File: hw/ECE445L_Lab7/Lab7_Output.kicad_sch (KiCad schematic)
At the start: 4 parts, among them Q1 IRLD024PBF, U2 Adafruit ST7735R

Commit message: finished preliminary pin assignment
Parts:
- removed Q1: IRLD024PBF, ECE445L:DIP920W60P254L490H457Q4N, symbol ECE445L:IRLD024PBF
- added M1, M2, M3, M4: Motor_DC, symbol Motor:Motor_DC
- added Q1, Q2, Q3, Q4: NTR4501NT1G, ECE445L:SOT96P237X111-3N, symbol ECE445L:NTR4501NT1G
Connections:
- new net: M3.2 (-), Q3.3 (D)
- new net: M4.2 (-), Q4.3 (D)
- new net: M2.2 (-), Q2.3 (D)
- new net: M1.2 (-), Q1.3 (D)
- new net GNDPWR: Q1.2 (S), Q2.2 (S), Q3.2 (S), Q4.2 (S)
- new net V_{g}: M1.1 (+), M2.1 (+), M3.1 (+), M4.1 (+)

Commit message: work on schem
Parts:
- added M5, M6: Motor_DC, symbol Motor:Motor_DC
- added M7: Solenoid_DC, symbol Motor:Motor_DC
- added Q5: NTR4501NT1G, ECE445L:SOT96P237X111-3N, symbol ECE445L:NTR4501NT1G
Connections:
- net GND: now also Q5.2 (S)
- net at D1.2 (A), LS1.2: now also Q5.3 (D)
- net uC_{2} - PA8: now reaches Q3.1 (G)
- net uC_{2} - PA10: now reaches Q4.1 (G)
- net uC_{2} - PA26: now reaches Q1.1 (G)
- net uC_{2} - PA23: now reaches Q2.1 (G)
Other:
- moved on the sheet: D1, LS1, M1, M3, M4, Q1, Q3, Q4

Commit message: mostly finished schem
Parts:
- added C7: 10u, Capacitor_SMD:C_0805_2012Metric_Pad1.18x1.45mm_HandSolder, symbol ECE445L:C
- added Q6, Q7, Q8: NTR4501NT1G, ECE445L:SOT96P237X111-3N, symbol ECE445L:NTR4501NT1G
- M1, M2, M3, M4, M7: footprint (none) -> Connector_JST:JST_PH_B2B-PH-K_1x02_P2.00mm_Vertical
- M_{flywheel,1}: renamed from M5; footprint (none) -> Connector_JST:JST_PH_B2B-PH-K_1x02_P2.00mm_Vertical
- M_{flywheel,2}: renamed from M6; footprint (none) -> Connector_JST:JST_PH_B2B-PH-K_1x02_P2.00mm_Vertical
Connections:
- net V_{g} is gone; now on net +12V: M1.1 (+), M2.1 (+), M3.1 (+), M4.1 (+)
- net +3V3: now also U2.2 (VCC)
- net GNDPWR: now also C7.2, Q6.2 (S), Q7.2 (S), Q8.2 (S)
- net +12V: now reaches M7.1 (+)
- net +12V: now also M_{flywheel,1}.1 (+), M_{flywheel,2}.1 (+)
- net at M7.2 (-): now also Q8.3 (D)
- net at M_{flywheel,2}.2 (-): now also Q7.3 (D)
- net uC_{2} - Speaker: now reaches Q5.1 (G)
- net at M_{flywheel,1}.2 (-): now also Q6.3 (D)
- net uC_{2} - PA10 renamed uC_{2} - Motor_{4}
- net uC_{2} - PA23 renamed uC_{2} - Motor_{2}
- net uC_{2} - PA26 renamed uC_{2} - Motor_{1}
- net uC_{2} - PA8 renamed uC_{2} - Motor_{3}
- new net uC_{2} - Flywheels: Q6.1 (G), Q7.1 (G)
- new net uC_{2} - Solenoid: Q8.1 (G)
- no-connect marks 0 -> 1
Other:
- moved on the sheet: M1, M3, M4, M7, M_{flywheel,1}, M_{flywheel,2}, Q1, Q3, Q4

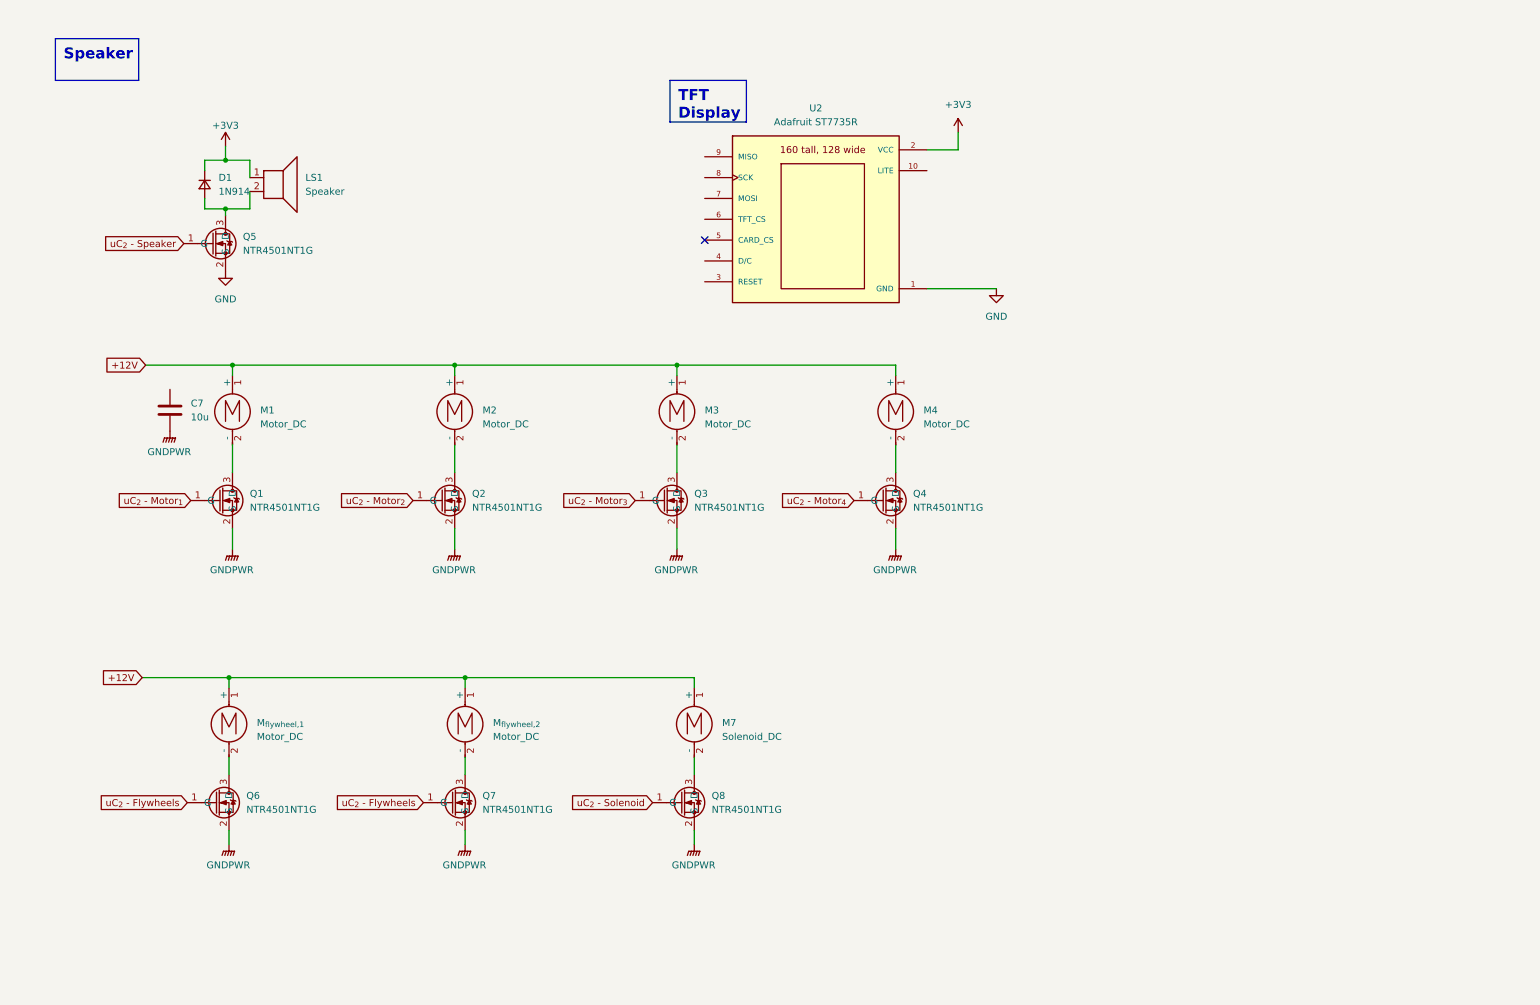
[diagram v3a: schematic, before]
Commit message: added reverse engineering for water atomizer
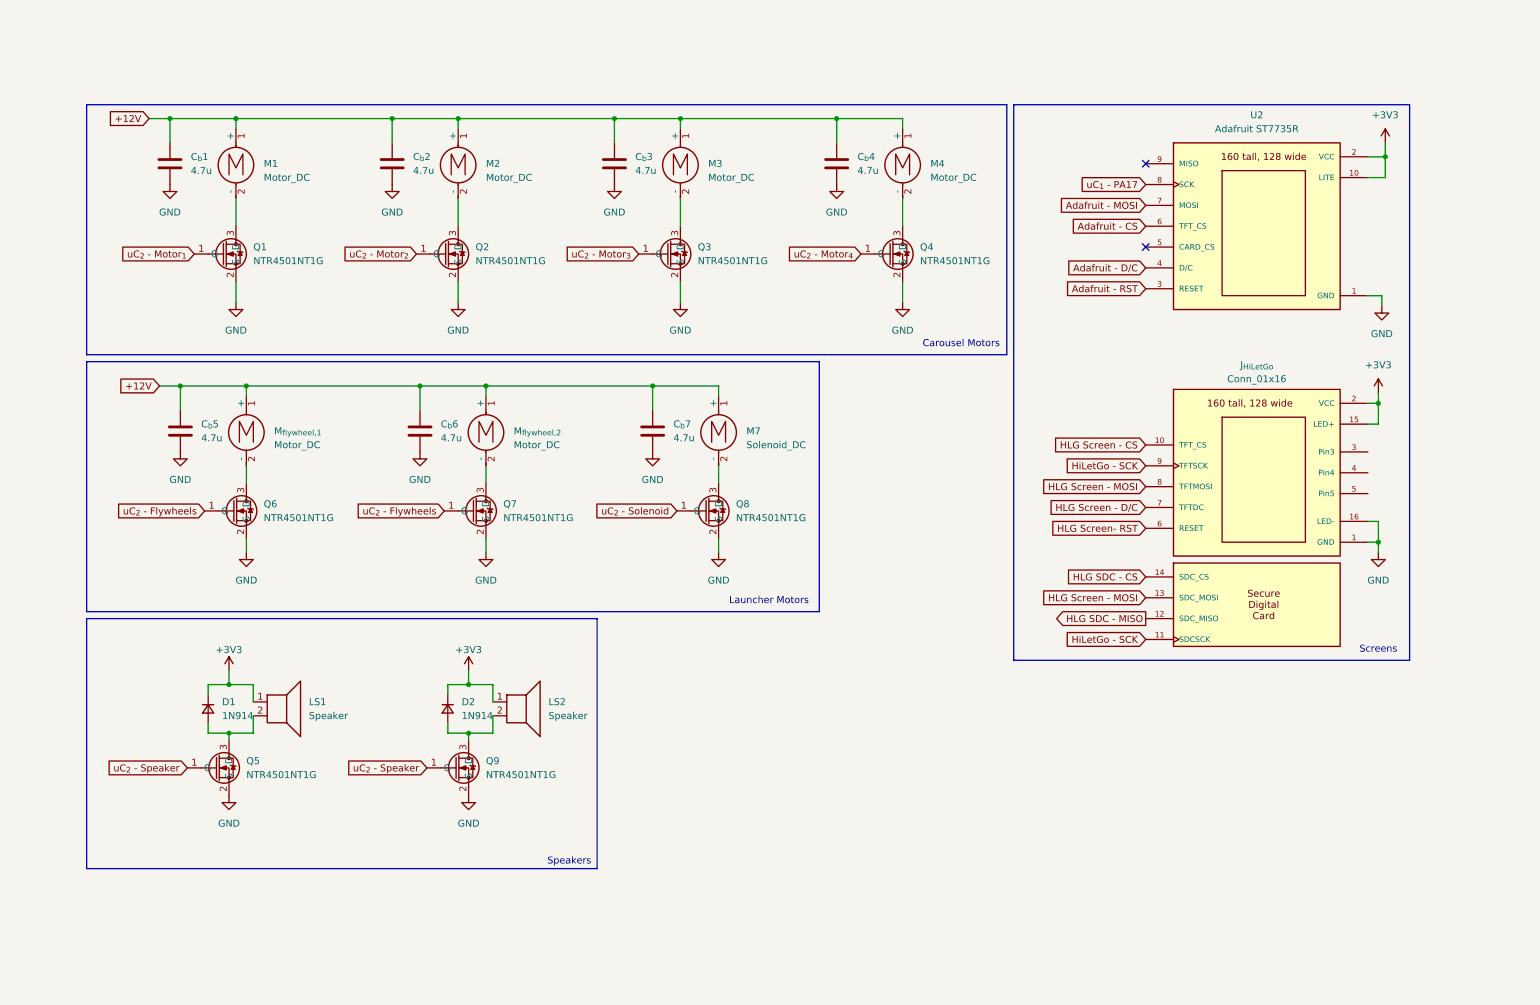
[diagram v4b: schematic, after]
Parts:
- added C_{b}2, C_{b}3, C_{b}4, C_{b}5, C_{b}6, C_{b}7: 4.7u, Capacitor_SMD:C_0805_2012Metric_Pad1.18x1.45mm_HandSolder, symbol ECE445L:C
- added D2: 1N914, Diode_THT:D_5W_P12.70mm_Horizontal, symbol Device:D_Small
- added J_{HiLetGo}: Conn_01x16, ECE445L:hiletgo_st7735r2, symbol ECE445L:HiLetGo_ST7735R
- added LS2: Speaker, ECE445L:PinHeader_1x02_P2.54mm_Vertical, symbol ECE445L:Speaker
- added Q9: NTR4501NT1G, ECE445L:SOT96P237X111-3N, symbol ECE445L:NTR4501NT1G
- C_{b}1: renamed from C7; value 10u -> 4.7u
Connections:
- net GNDPWR is gone; now on net GND: C_{b}1.2, Q1.2 (S), Q2.2 (S), Q3.2 (S), Q4.2 (S), Q6.2 (S), Q7.2 (S), Q8.2 (S)
- net +12V: now also C_{b}1.1, C_{b}2.1, C_{b}3.1, C_{b}4.1, C_{b}5.1, C_{b}6.1, C_{b}7.1
- net +3V3: now also U2.10 (LITE), D2.1 (K), J_{HiLetGo}.15 (LED+), J_{HiLetGo}.2 (VCC), LS2.1
- net GND: now also C_{b}2.2, C_{b}3.2, C_{b}4.2, C_{b}5.2, C_{b}6.2, C_{b}7.2, J_{HiLetGo}.1 (GND), J_{HiLetGo}.16 (LED-), Q9.2 (S)
- net uC_{2} - Speaker: now also Q9.1 (G)
- net Adafruit - RST: now reaches U2.3 (RESET)
- net Adafruit - D/C: now reaches U2.4 (D/C)
- net Adafruit - CS: now reaches U2.6 (TFT_CS)
- net Adafruit - MOSI: now reaches U2.7 (MOSI)
- net uC_{1} - PA17: now reaches U2.8 (SCK)
- new net: D2.2 (A), LS2.2, Q9.3 (D)
- new net HLG SDC - CS: J_{HiLetGo}.14 (SDC_CS)
- new net HLG SDC - MISO: J_{HiLetGo}.12 (SDC_MISO)
- new net HLG Screen - CS: J_{HiLetGo}.10 (TFT_CS)
- new net HLG Screen - D/C: J_{HiLetGo}.7 (TFTDC)
- new net HLG Screen - MOSI: J_{HiLetGo}.13 (SDC_MOSI), J_{HiLetGo}.8 (TFTMOSI)
- new net HLG Screen- RST: J_{HiLetGo}.6 (RESET)
- new net HiLetGo - SCK: J_{HiLetGo}.11 (SDCSCK), J_{HiLetGo}.9 (TFTSCK)
- no-connect marks 1 -> 2
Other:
- note added: "Carousel Motors"
- note added: "Launcher Motors"
- note added: "Screens"
- note added: "Speakers"
- company: (none) -> ECE445L
- title: (none) -> Output
- moved on the sheet: C_{b}1, D1, LS1, M1, M2, M3, M4, M7, M_{flywheel,1}, M_{flywheel,2}, Q1, Q2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

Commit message: almost finished with schem
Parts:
- removed J_{HiLetGo}: Conn_01x16, ECE445L:hiletgo_st7735r2, symbol ECE445L:HiLetGo_ST7735R
- added J_{LED,G1}, J_{LED,G2}, J_{LED,G3}: Conn_01x02, Connector_PinSocket_2.54mm:PinSocket_1x02_P2.54mm_Vertical, symbol Connector_Generic:Conn_01x02
- added J_{atomizer}: Conn_01x03, Connector_PinSocket_2.54mm:PinSocket_1x03_P2.54mm_Vertical, symbol Connector_Generic:Conn_01x03
- added U5: HiLetGo_ST7735R, ECE445L:hiletgo_st7735r2, symbol ECE445L:HiLetGo_ST7735R
- M1, M2, M3, M4, M_{flywheel,1}, M_{flywheel,2}: value Motor_DC -> Motor _DC
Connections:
- net +3V3: now also J_{atomizer}.2 (Pin_2), U5.15 (LED+), U5.2 (VCC)
- net GND: now also J_{atomizer}.3 (Pin_3), U5.1 (GND), U5.16 (LED-)
- net HLG SDC - CS: now also U5.14 (SDC_CS)
- net HLG SDC - MISO: now also U5.12 (SDC_MISO)
- net HLG Screen - CS: now also U5.10 (TFT_CS)
- net HLG Screen - D/C: now also U5.7 (TFTDC)
- net HLG Screen - MOSI: now also U5.13 (SDC_MOSI), U5.8 (TFTMOSI)
- net HLG Screen- RST: now also U5.6 (RESET)
- net HiLetGo - SCK: now also U5.11 (SDCSCK), U5.9 (TFTSCK)
- net uC_{2} - Motor_{1} renamed uC_{2} - Motor _{1}
- net uC_{2} - Motor_{2} renamed uC_{2} - Motor _{2}
- net uC_{2} - Motor_{3} renamed uC_{2} - Motor _{3}
- net uC_{2} - Motor_{4} renamed uC_{2} - Motor _{4}
- new net uC_{2} - Smoke: J_{atomizer}.1 (Pin_1)
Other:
- note added: "Misc. Outputs"

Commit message: finished prelim schem
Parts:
- removed D1, D2: 1N914, Diode_THT:D_5W_P12.70mm_Horizontal, symbol Device:D_Small
- removed J_{LED,G1}, J_{LED,G2}, J_{LED,G3}: Conn_01x02, Connector_PinSocket_2.54mm:PinSocket_1x02_P2.54mm_Vertical, symbol Connector_Generic:Conn_01x02
- removed J_{atomizer}: Conn_01x03, Connector_PinSocket_2.54mm:PinSocket_1x03_P2.54mm_Vertical, symbol Connector_Generic:Conn_01x03
- removed LS1, LS2: Speaker, ECE445L:PinHeader_1x02_P2.54mm_Vertical, symbol ECE445L:Speaker
- removed U2: Adafruit ST7735R, ECE445L:adafruit_st7735r2, symbol ECE445L:Adafruit_ST7735R
- removed U5: HiLetGo_ST7735R, ECE445L:hiletgo_st7735r2, symbol ECE445L:HiLetGo_ST7735R
- added C_{b}10, C_{b}11, C_{b}12, C_{b}5, C_{b}6, C_{b}7, C_{b}8, C_{b}9: 4.7u, Capacitor_SMD:C_0603_1608Metric_Pad1.08x0.95mm_HandSolder, symbol ECE445L:C
- added D_{flyback}1, D_{flyback}10, D_{flyback}11, D_{flyback}12, D_{flyback}13, D_{flyback}14, D_{flyback}15, D_{flyback}2, D_{flyback}3, D_{flyback}4, D_{flyback}5, D_{flyback}6, D_{flyback}7, D_{flyback}8, D_{flyback}9: 12V, Diode_SMD:D_SOD-523, symbol Device:D_Small
- added Flywheel_V_{d}1, Flywheel_V_{d}2, Flywheels_In1, Motor_In1, Motor_In10, Motor_In11, Motor_In12, Motor_In15, Motor_In2, Motor_In3, Motor_In4, Motor_In5, Motor_In6, Motor_In7, Motor_In8, Motor_In9, Motor_V_{d}1, Motor_V_{d}10, Motor_V_{d}11, Motor_V_{d}12, Motor_V_{d}2, Motor_V_{d}3, Motor_V_{d}4, Motor_V_{d}5, Motor_V_{d}6, Motor_V_{d}7, Motor_V_{d}8, Motor_V_{d}9, Solenoid_V_{d}1: TestPoint, TestPoint:TestPoint_Keystone_5010-5014_Multipurpose, symbol Connector:TestPoint
- added M10, M11, M12, M5, M6, M7, M8, M9: Motor_DC, Connector_AMASS:AMASS_XT30U-M_1x02_P5.0mm_Vertical, symbol Motor:Motor_DC
- added Q10, Q11, Q12, Q6, Q7, Q8: NTR4501NT1G, ECE445L:SOT96P237X111-3N, symbol ECE445L:NTR4501NT1G
- added R_{choke}1, R_{choke}10, R_{choke}11, R_{choke}12, R_{choke}13, R_{choke}14, R_{choke}15, R_{choke}2, R_{choke}3, R_{choke}4, R_{choke}5, R_{choke}6, R_{choke}7, R_{choke}8, R_{choke}9: 680, Resistor_SMD:R_0603_1608Metric_Pad0.98x0.95mm_HandSolder, symbol Device:R
- added R_{gate}1, R_{gate}10, R_{gate}11, R_{gate}12, R_{gate}13, R_{gate}14, R_{gate}15, R_{gate}2, R_{gate}3, R_{gate}4, R_{gate}5, R_{gate}6, R_{gate}7, R_{gate}8, R_{gate}9: 0.25, Resistor_SMD:R_0603_1608Metric_Pad0.98x0.95mm_HandSolder, symbol Device:R
- added SW_{bypass}1, SW_{bypass}10, SW_{bypass}11, SW_{bypass}12, SW_{bypass}13, SW_{bypass}14, SW_{bypass}15, SW_{bypass}2, SW_{bypass}3, SW_{bypass}4, SW_{bypass}5, SW_{bypass}6, SW_{bypass}7, SW_{bypass}8, SW_{bypass}9: NO, ECE445L:SW_PUSH_6mm, symbol ECE445L:SW_Push
- C_{b}1, C_{b}2, C_{b}3, C_{b}4: footprint Capacitor_SMD:C_0805_2012Metric_Pad1.18x1.45mm_HandSolder -> Capacitor_SMD:C_0603_1608Metric_Pad1.08x0.95mm_HandSolder; Distributor (none) -> Mouser; Manufacturer (none) -> Walsin; Manufacturer_Part_Number (none) -> 0805X475M250CT; Mouser Part Number (none) -> 791-0805X475M250CT
- C_{b}13: renamed from C_{b}5; footprint Capacitor_SMD:C_0805_2012Metric_Pad1.18x1.45mm_HandSolder -> Capacitor_SMD:C_0603_1608Metric_Pad1.08x0.95mm_HandSolder; Distributor (none) -> Mouser; Manufacturer (none) -> Walsin; Manufacturer_Part_Number (none) -> 0805X475M250CT; Mouser Part Number (none) -> 791-0805X475M250CT
- C_{b}14: renamed from C_{b}6; footprint Capacitor_SMD:C_0805_2012Metric_Pad1.18x1.45mm_HandSolder -> Capacitor_SMD:C_0603_1608Metric_Pad1.08x0.95mm_HandSolder; Distributor (none) -> Mouser; Manufacturer (none) -> Walsin; Manufacturer_Part_Number (none) -> 0805X475M250CT; Mouser Part Number (none) -> 791-0805X475M250CT
- C_{b}15: renamed from C_{b}7; footprint Capacitor_SMD:C_0805_2012Metric_Pad1.18x1.45mm_HandSolder -> Capacitor_SMD:C_0603_1608Metric_Pad1.08x0.95mm_HandSolder; Distributor (none) -> Mouser; Manufacturer (none) -> Walsin; Manufacturer_Part_Number (none) -> 0805X475M250CT; Mouser Part Number (none) -> 791-0805X475M250CT
- M1, M2, M3, M4: value Motor _DC -> Motor_DC; footprint Connector_JST:JST_PH_B2B-PH-K_1x02_P2.00mm_Vertical -> Connector_AMASS:AMASS_XT30U-M_1x02_P5.0mm_Vertical; Distributor (none) -> Amazon; Manufacturer (none) -> Coliao
- M_{feeder}1: renamed from M7; value Solenoid_DC -> Solenoid; Distributor (none) -> Amazon; Manufacturer (none) -> Heschen
- M_{flywheel,1}1: renamed from M_{flywheel,1}; value Motor _DC -> Motor_DC; footprint Connector_JST:JST_PH_B2B-PH-K_1x02_P2.00mm_Vertical -> Connector_AMASS:AMASS_XT30U-M_1x02_P5.0mm_Vertical; Distributor (none) -> Amazon; Manufacturer (none) -> AUTOTOOLHOME
- M_{flywheel,2}1: renamed from M_{flywheel,2}; value Motor _DC -> Motor_DC; footprint Connector_JST:JST_PH_B2B-PH-K_1x02_P2.00mm_Vertical -> Connector_AMASS:AMASS_XT30U-M_1x02_P5.0mm_Vertical; Distributor (none) -> Amazon; Manufacturer (none) -> AUTOTOOLHOME
- Q1, Q2, Q3, Q4, Q5, Q9: Distributor (none) -> Checkout; Manufacturer (none) -> onsemi
- Q13: renamed from Q6; Distributor (none) -> Checkout; Manufacturer (none) -> onsemi
- Q14: renamed from Q7; Distributor (none) -> Checkout; Manufacturer (none) -> onsemi
- Q15: renamed from Q8; Distributor (none) -> Checkout; Manufacturer (none) -> onsemi
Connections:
- net +12V: now also C_{b}10.1, C_{b}11.1, C_{b}12.1, C_{b}5.1, C_{b}6.1, C_{b}7.1, C_{b}8.1, C_{b}9.1, D_{flyback}1.1 (K), D_{flyback}10.1 (K), D_{flyback}11.1 (K), D_{flyback}12.1 (K), D_{flyback}13.1 (K), D_{flyback}14.1 (K), D_{flyback}15.1 (K), D_{flyback}2.1 (K), D_{flyback}3.1 (K), D_{flyback}4.1 (K), D_{flyback}5.1 (K), D_{flyback}6.1 (K), D_{flyback}7.1 (K), D_{flyback}8.1 (K), D_{flyback}9.1 (K), M10.1 (+), M11.1 (+), M12.1 (+), M5.1 (+), M6.1 (+), M7.1 (+), M8.1 (+), M9.1 (+)
- net +3V3: now also SW_{bypass}1.1, SW_{bypass}10.1, SW_{bypass}11.1, SW_{bypass}12.1, SW_{bypass}13.1, SW_{bypass}14.1, SW_{bypass}15.1, SW_{bypass}2.1, SW_{bypass}3.1, SW_{bypass}4.1, SW_{bypass}5.1, SW_{bypass}6.1, SW_{bypass}7.1, SW_{bypass}8.1, SW_{bypass}9.1
- net GND: now also C_{b}10.2, C_{b}11.2, C_{b}12.2, C_{b}5.2, C_{b}6.2, C_{b}7.2, C_{b}8.2, C_{b}9.2, Q10.2 (S), Q11.2 (S), Q12.2 (S), Q6.2 (S), Q7.2 (S), Q8.2 (S)
- net V_{d,motor 5}: now reaches Q5.3 (D)
- net V_{d,motor 5}: now also D_{flyback}5.2 (A), M5.2 (-), Motor_V_{d}5.1
- net V_{d,motor 3}: now reaches M3.2 (-), Q3.3 (D)
- net V_{d,motor 3}: now also D_{flyback}3.2 (A), Motor_V_{d}3.1
- net V_{d,motor 9}: now reaches Q9.3 (D)
- net V_{d,motor 9}: now also D_{flyback}9.2 (A), M9.2 (-), Motor_V_{d}9.1
- net V_{d,solenoid}: now reaches M_{feeder}1.2 (-), Q15.3 (D)
- net V_{d,solenoid}: now also D_{flyback}15.2 (A), Solenoid_V_{d}1.1
- net V_{d,flywheel 2}: now reaches M_{flywheel,2}1.2 (-), Q14.3 (D)
- net V_{d,flywheel 2}: now also D_{flyback}14.2 (A), Flywheel_V_{d}2.1
- net V_{d,motor 4}: now reaches M4.2 (-), Q4.3 (D)
- net V_{d,motor 4}: now also D_{flyback}4.2 (A), Motor_V_{d}4.1
- net V_{d,motor 2}: now reaches M2.2 (-), Q2.3 (D)
- net V_{d,motor 2}: now also D_{flyback}2.2 (A), Motor_V_{d}2.1
- net V_{d,motor 1}: now reaches M1.2 (-), Q1.3 (D)
- net V_{d,motor 1}: now also D_{flyback}1.2 (A), Motor_V_{d}1.1
- net V_{d,flywheel 1}: now reaches M_{flywheel,1}1.2 (-), Q13.3 (D)
- net V_{d,flywheel 1}: now also D_{flyback}13.2 (A), Flywheel_V_{d}1.1
- net uC_{2} - Flywheels: no longer names the net of Q14.1 (G)
- net uC_{2} - Flywheels: now also R_{choke}14.1, R_{gate}14.1; no longer Q13.1 (G)
- net uC_{2} - Motor _{1}: no longer names the net of Q1.1 (G)
- net uC_{2} - Motor _{1}: now also R_{choke}1.1, R_{gate}1.1
- net uC_{2} - Motor _{2}: no longer names the net of Q2.1 (G)
- net uC_{2} - Motor _{2}: now also R_{choke}2.1, R_{gate}2.1
- net uC_{2} - Motor _{3}: no longer names the net of Q3.1 (G)
- net uC_{2} - Motor _{3}: now also R_{choke}3.1, R_{gate}3.1
- net uC_{2} - Motor _{4}: no longer names the net of Q4.1 (G)
- net uC_{2} - Motor _{4}: now also R_{choke}4.1, R_{gate}4.1
- net uC_{2} - Solenoid: no longer names the net of Q15.1 (G)
- net uC_{2} - Solenoid: now also R_{choke}15.1, R_{gate}15.1
- net uC_{2} - Speaker: no longer names the net of Q5.1 (G)
- net uC_{2} - Speaker: now also R_{choke}5.1, R_{gate}5.1; no longer Q9.1 (G)
- new net: Q11.1 (G), R_{choke}11.1, R_{gate}11.1
- new net: R_{choke}6.2, SW_{bypass}6.2
- new net: Q8.1 (G), R_{choke}8.1, R_{gate}8.1
- new net: Q10.1 (G), R_{choke}10.1, R_{gate}10.1
- new net: R_{choke}2.2, SW_{bypass}2.2
- new net: Q6.1 (G), R_{choke}6.1, R_{gate}6.1
- new net: Q12.1 (G), R_{choke}12.1, R_{gate}12.1
- new net: R_{choke}4.2, SW_{bypass}4.2
- new net: R_{choke}9.2, SW_{bypass}9.2
- new net: Q7.1 (G), R_{choke}7.1, R_{gate}7.1
- new net: Q9.1 (G), R_{choke}9.1, R_{gate}9.1
- new net: R_{choke}11.2, SW_{bypass}11.2
- new net: R_{choke}5.2, SW_{bypass}5.2
- new net: R_{choke}14.2, SW_{bypass}14.2
- new net: R_{choke}15.2, SW_{bypass}15.2
- new net: R_{choke}7.2, SW_{bypass}7.2
- new net: R_{choke}3.2, SW_{bypass}3.2
- new net: R_{choke}12.2, SW_{bypass}12.2
- new net: R_{choke}10.2, SW_{bypass}10.2
- new net: Q13.1 (G), R_{choke}13.1, R_{gate}13.1
- new net: R_{choke}8.2, SW_{bypass}8.2
- new net: R_{choke}1.2, SW_{bypass}1.2
- new net: R_{choke}13.2, SW_{bypass}13.2
- new net Flywheels: Flywheels_In1.1, R_{gate}13.2, R_{gate}14.2
- new net Motor_{10}: Motor_In11.1, R_{gate}10.2
- new net Motor_{11}: Motor_In10.1, R_{gate}11.2
- new net Motor_{12}: Motor_In12.1, R_{gate}12.2
- new net Motor_{1}: Motor_In1.1, R_{gate}1.2
- new net Motor_{2}: Motor_In2.1, R_{gate}2.2
- new net Motor_{3}: Motor_In3.1, R_{gate}3.2
- new net Motor_{4}: Motor_In4.1, R_{gate}4.2
- new net Motor_{5}: Motor_In5.1, R_{gate}5.2
- new net Motor_{6}: Motor_In7.1, R_{gate}6.2
- new net Motor_{7}: Motor_In6.1, R_{gate}7.2
- new net Motor_{8}: Motor_In8.1, R_{gate}8.2
- new net Motor_{9}: Motor_In9.1, R_{gate}9.2
- new net Solenoid: Motor_In15.1, R_{gate}15.2
- new net V_{d,motor 10}: D_{flyback}10.2 (A), M10.2 (-), Motor_V_{d}11.1, Q10.3 (D)
- new net V_{d,motor 11}: D_{flyback}11.2 (A), M11.2 (-), Motor_V_{d}10.1, Q11.3 (D)
- new net V_{d,motor 12}: D_{flyback}12.2 (A), M12.2 (-), Motor_V_{d}12.1, Q12.3 (D)
- new net V_{d,motor 6}: D_{flyback}6.2 (A), M6.2 (-), Motor_V_{d}7.1, Q6.3 (D)
- new net V_{d,motor 7}: D_{flyback}7.2 (A), M7.2 (-), Motor_V_{d}6.1, Q7.3 (D)
- new net V_{d,motor 8}: D_{flyback}8.2 (A), M8.2 (-), Motor_V_{d}8.1, Q8.3 (D)
- no-connect marks 2 -> 0
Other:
- note added: "Carousel/Coil Motors"
- note added: "Coil Motors"
- note added: "Test Points"
- note removed: "Carousel Motors"
- note removed: "Misc. Outputs"
- note removed: "Screens"
- note removed: "Speakers"
- moved on the sheet: C_{b}1, C_{b}13, C_{b}14, C_{b}15, C_{b}2, C_{b}3, C_{b}4, M1, M2, M3, M4, M_{feeder}1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
